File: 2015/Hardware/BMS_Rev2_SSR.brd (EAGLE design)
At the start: 51.8 x 82.5 mm, 13 parts

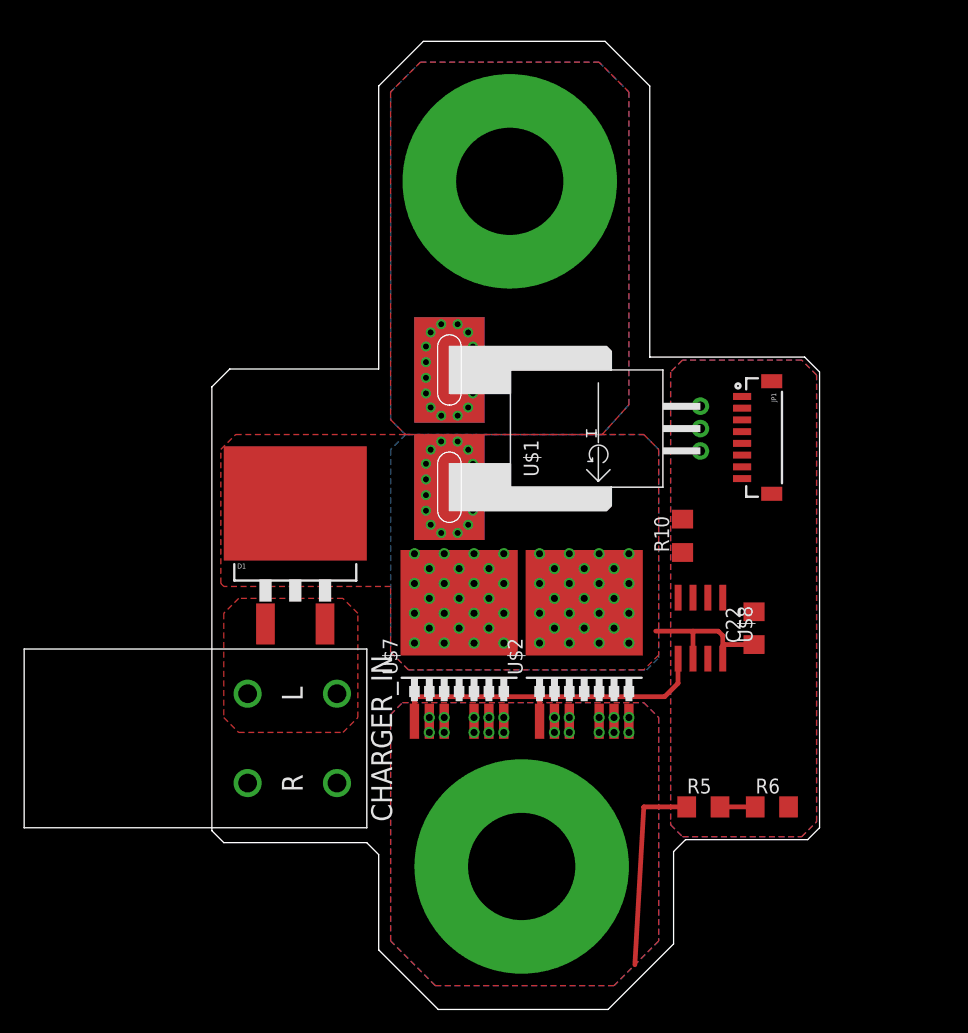
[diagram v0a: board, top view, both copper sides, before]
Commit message: Finished SSR board in Rev 2
The physical board is no longer shaped like a feminine hygiene product.
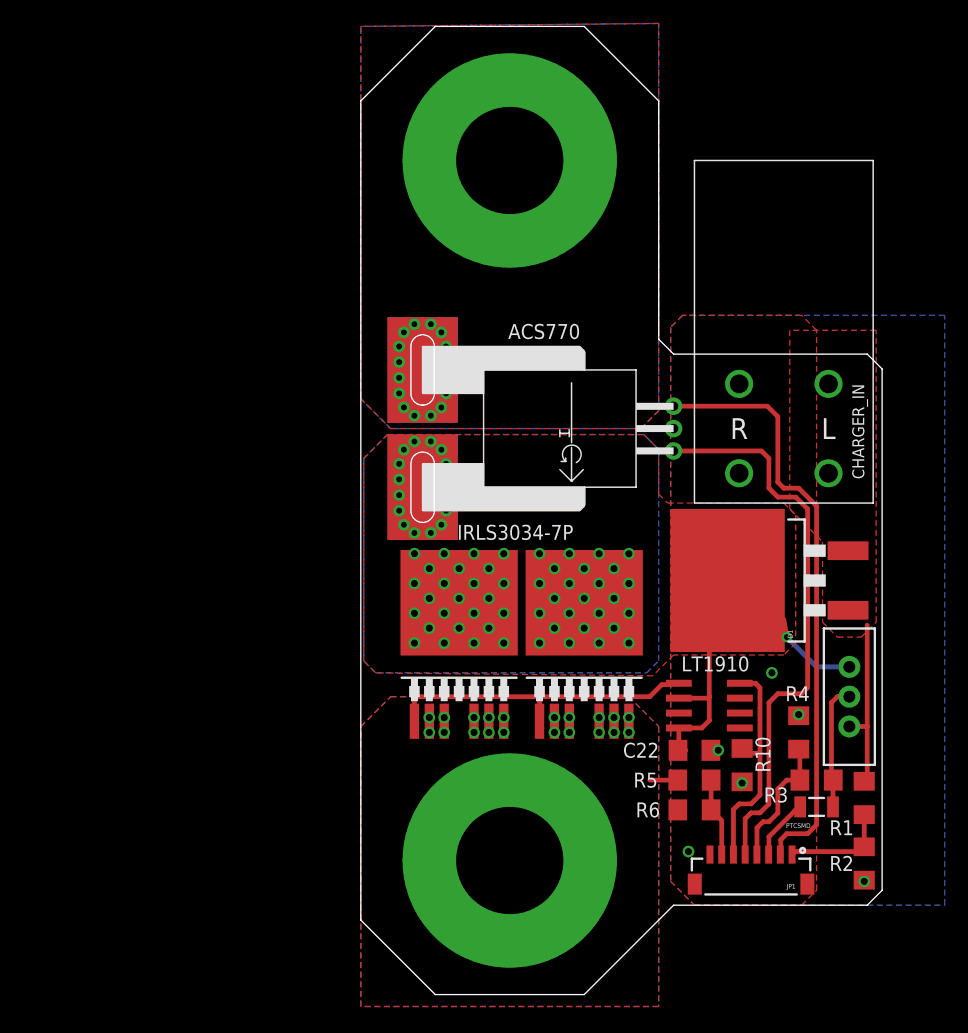
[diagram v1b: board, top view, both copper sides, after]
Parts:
- added F1: PTCSMD, SparkFun-PowerIC:PTC-1206
- added R1, R3: 60kΩ, resistor:R1206
- added R2, R4: 10kΩ, resistor:R1206
- added S1: (no value), SparkFun-Electromechanical:SWITCH-SPDT
- moved CHARGER_IN 49.5 mm to (48.8, 48.3), turned to 180 degrees
- moved D1 39.1 mm to (46.0, 35.3), turned to 90 degrees
- moved JP1 35.6 mm to (46.0, 11.9), turned to 180 degrees
- moved R10 20.2 mm to (45.2, 19.6), turned to 270 degrees
- moved C22 11.6 mm to (41.1, 20.8), turned to 0 degrees
- moved U$8 6.65 mm to (42.4, 24.6), turned to 90 degrees
- moved R6 6.61 mm to (41.1, 15.7), turned to 180 degrees
- moved R5 2.41 mm to (41.1, 18.3)
- moved U$1 2.29 mm to (39.4, 48.3)
- moved V_ARRAY 1.78 mm to (25.4, 71.1)
- moved V_OUT 1.14 mm to (25.4, 11.4)
- renumbered U$2 to IRLS3034-7P.2, U$7 to IRLS3034-7P
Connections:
- removed net N$8: CHARGER_IN.L1, CHARGER_IN.L2, D1.1, D1.2
- new net LOGIC_POWER: F1.2, JP1.3
- new net N$4: CHARGER_IN.L1, CHARGER_IN.L2, D1.1, D1.2, R1.1, S1.3
- new net N$6: F1.1, R3.2, S1.2
- new net V_CHECK: JP1.4, R3.1, R4.2
- new net V_CHG: JP1.1, R1.2, R2.1
- net 5V: now also JP1.5; no longer JP1.1
- net GATE: now also JP1.6; no longer JP1.3
- net GND: now also R2.2, R4.1
- net N$3: now also S1.1
- net V_OUT: now also JP1.7
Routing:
- net I_ARRAY: track 0.00 -> 51.0 mm
- net 5V: track 0.00 -> 48.3 mm
- net GATE: track 0.00 -> 19.4 mm
- net N$4: track 0.00 -> 15.0 mm
- net N$1: track 17.1 -> 2.39 mm
- net N$6: track 0.00 -> 12.0 mm
- net V_CHECK: track 0.00 -> 11.5 mm
- net V_CHG: track 0.00 -> 9.57 mm
- net N$3: track 12.9 -> 22.3 mm, vias 50 -> 51
- net LOGIC_POWER: track 0.00 -> 5.37 mm
- net V_OUT: track 3.00 -> 6.72 mm
- net N$5: track 29.1 -> 27.0 mm
- net GND: track 0.00 -> 0.10 mm, vias 0 -> 6
- added copper zone on layer 1, net N$4
- removed copper zone on layer 1, net N$8
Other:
- board size 51.8 x 82.5 mm -> 44.5 x 82.5 mm

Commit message: Widened SSR board to be ok with 2 oz copper
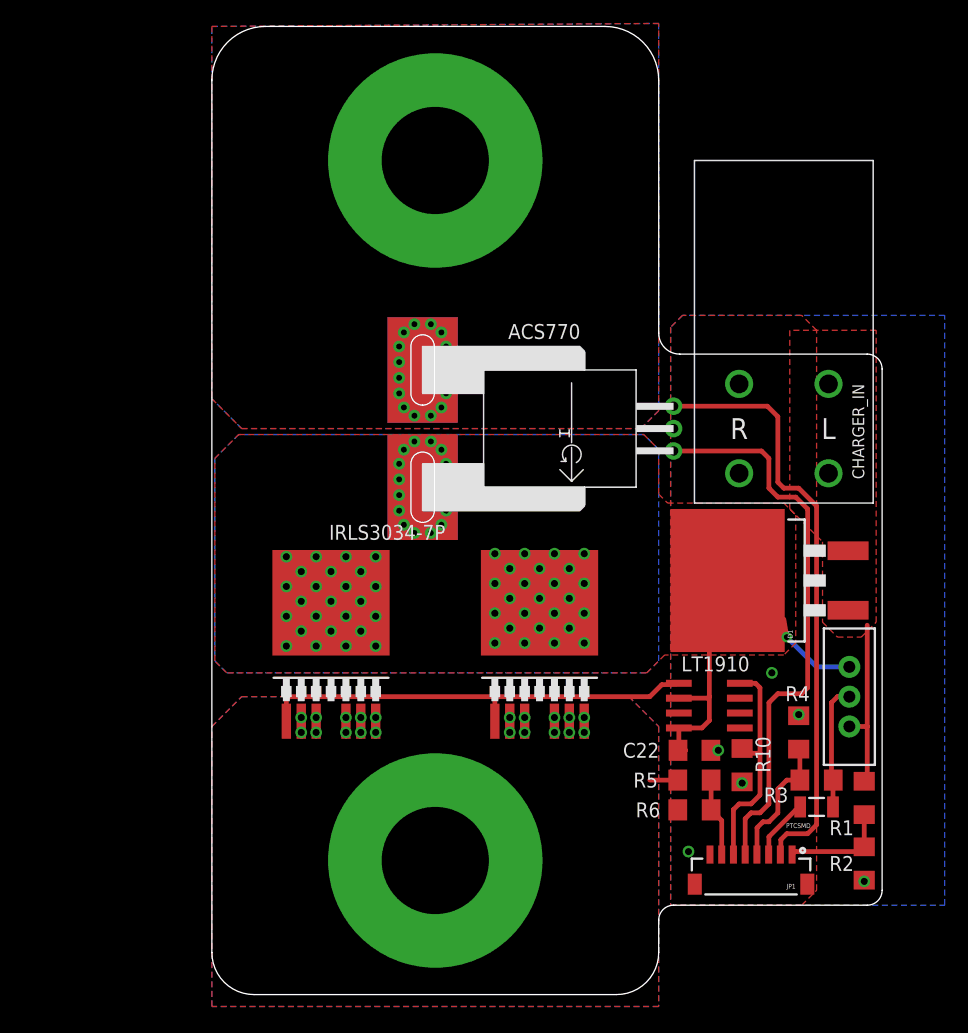
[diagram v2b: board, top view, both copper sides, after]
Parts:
- moved IRLS3034-7P 10.9 mm to (10.2, 32.5)
- moved V_ARRAY 6.35 mm to (19.1, 71.1)
- moved V_OUT 6.35 mm to (19.1, 11.4)
- moved IRLS3034-7P.2 3.81 mm to (27.9, 32.5)
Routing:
- net N$5: track 27.0 -> 37.9 mm
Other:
- board size 44.5 x 82.5 mm -> 57.1 x 82.5 mm
